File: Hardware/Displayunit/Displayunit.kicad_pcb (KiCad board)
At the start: 4 copper layers, 155 x 64.8 mm, 124 parts, among them IC1 TSC2007, IC2 MX25LM51245GXDI00, IC3 IS66WVH8M8BLL-100B1LI_0, J1 8P8C_Shielded, J2 8P8C_Shielded, J3 54104-4031, J4 Conn_ARM_JTAG_SWD_20, J5 52271-0679, J6 Conn_02x06_Odd_Even, J7 WAGO_Klemmleiste_2-pol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

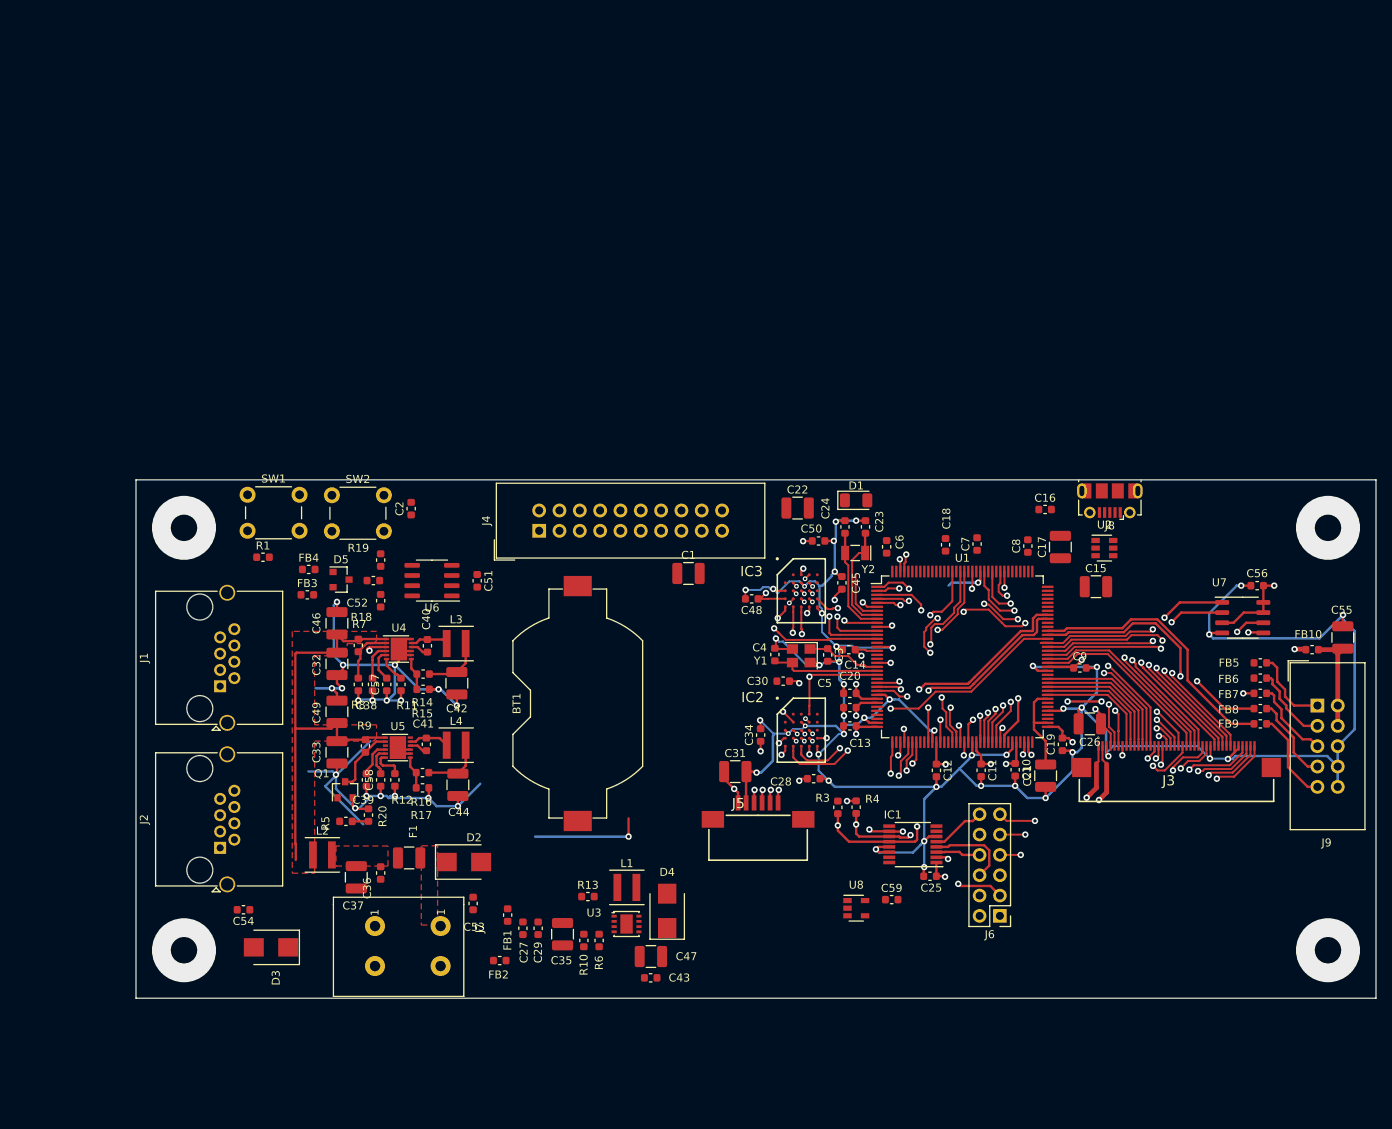
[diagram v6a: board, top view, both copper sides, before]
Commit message: Displayboard fertig layoutet, kleinere Fehler beseitigt, WomoLin Biblothek senkrechter Würth RJ 45 zugefügt
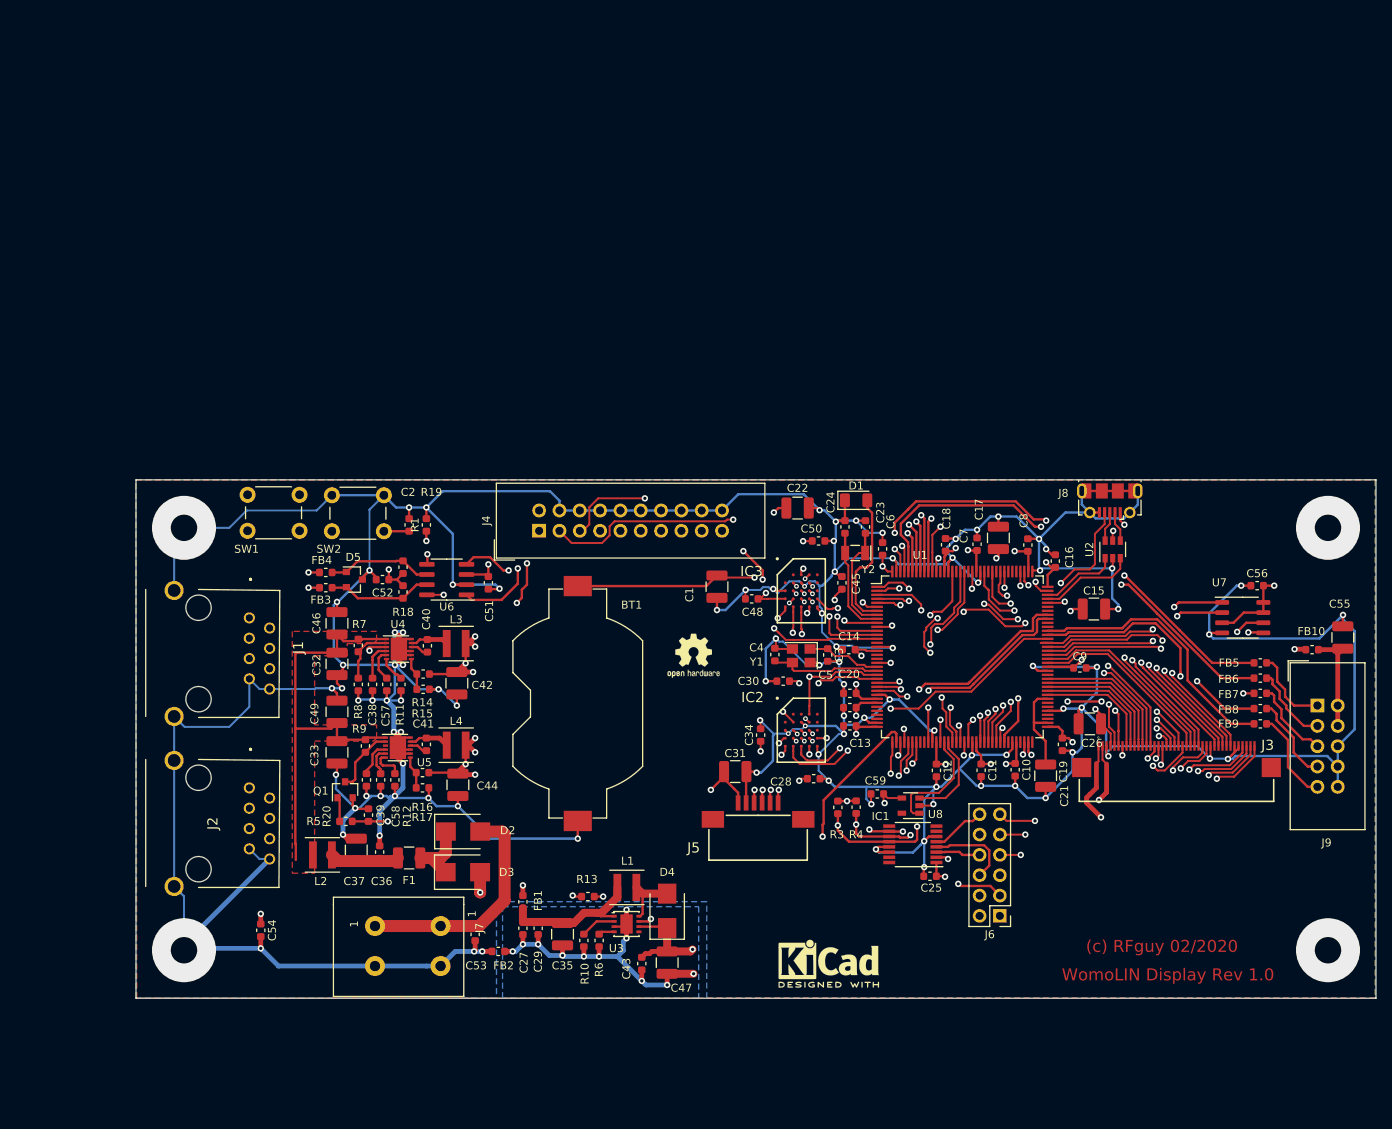
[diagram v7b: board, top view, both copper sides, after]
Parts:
- added REF**: OSHW-Logo2_7.3x6mm_SilkScreen, Symbol:OSHW-Logo2_7.3x6mm_SilkScreen, F.Cu at (131.7, 71.0)
- added REF**: KiCad-Logo2_5mm_SilkScreen, Symbol:KiCad-Logo2_5mm_SilkScreen, F.Cu at (148.6, 109.5)
- IC2: value MX25LM51245GXDI00 -> (none)
- IC3: value IS66WVH8M8BLL-100B1LI_0 -> (none)
- J1, J2: value 8P8C_Shielded -> 615008138221; footprint Connector_RJ:RJ45_Amphenol_RJHSE5380 -> Womo-Lin:615008138221
- J3: value 54104-4031 -> (none)
- J5: value 52271-0679 -> (none)
- moved D3 25.8 mm to (102.9, 98.0), turned to 0 degrees
- moved R1 20.8 mm to (98.3, 54.6), turned to 90 degrees
- moved U8 14.5 mm to (158.8, 89.7), turned to 180 degrees
- moved C59 13.3 mm to (154.7, 88.3), turned to 180 degrees
- moved J1 9.29 mm to (76.2, 66.3), turned to 270 degrees
- moved J2 8.33 mm to (76.2, 87.5), turned to 270 degrees
- moved C17 7.83 mm to (169.8, 56.3)
- moved C16 6.58 mm to (176.9, 59.2), turned to 90 degrees
- moved C1 3.92 mm to (134.6, 62.4), turned to 270 degrees
- moved C53 3.87 mm to (104.4, 105.8)
- moved D2 3.81 mm to (102.9, 93.0)
- moved C37 3.43 mm to (89.5, 95.3), turned to 90 degrees
- moved C54 3.35 mm to (77.6, 105.3), turned to 270 degrees
- moved R18 3.00 mm to (95.4, 63.0)
- moved R19 2.93 mm to (95.4, 59.9)
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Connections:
- U1 pad 135: Wakeup -> 3VA_EN
- U1 pad 24: Net-(U1-Pad24) -> CAN_STB
- U1 pad 38: LCD_BL_CTR -> LCD_BL_CTRL
- U2 pad 1: USB_D- -> USB_D+
- U2 pad 3: USB_D+ -> USB_D-
- U2 pad 4: Net-(J8-Pad3) -> Net-(J8-Pad2)
- U2 pad 6: Net-(J8-Pad2) -> Net-(J8-Pad3)
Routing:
- net GND: track 483.3 -> 889.5 mm, vias 66 -> 99
- net +3V3: track 202.8 -> 408.3 mm, vias 22 -> 36
- net 3VA_EN: track 2.03 -> 110.5 mm, vias 0 -> 4
- net Boot0: track 0.00 -> 100.8 mm, vias 0 -> 2
- net Control+: track 0.00 -> 82.5 mm, vias 0 -> 2
- net JTAG_TMS: track 0.00 -> 71.5 mm, vias 0 -> 1
- net USART1_TX: track 0.00 -> 70.2 mm, vias 0 -> 2
- net JTAG_TDI: track 0.00 -> 70.1 mm, vias 0 -> 2
- net CAN_STB: track 0.00 -> 67.4 mm, vias 0 -> 2
- net USART1_RX: track 0.00 -> 67.1 mm, vias 0 -> 2
- net JTAG_TCK: track 0.00 -> 67.0 mm, vias 0 -> 1
- net +3.3VA: track 87.6 -> 154.3 mm, vias 4 -> 10
- net RESET: track 31.8 -> 96.7 mm, vias 2 -> 5
- net EXT_1: track 0.00 -> 62.8 mm, vias 0 -> 4
- net EXT_2: track 0.00 -> 60.4 mm, vias 0 -> 2
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- added copper zone on In2.Cu, net +3.3VA
- added copper zone on In2.Cu, net +3V3
- added copper zone on B.Cu, net GND
- added copper zone on F.Cu, net GND
- added copper zone on B.Cu, net LCD_LED-K
- removed copper zone on F.Cu, net Net-(C36-Pad1)
- removed copper zone on F.Cu, net Net-(D2-Pad1)
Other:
- board text added: "(c) RFguy 02/2020"
- board text added: "WomoLIN Display Rev 1.0"

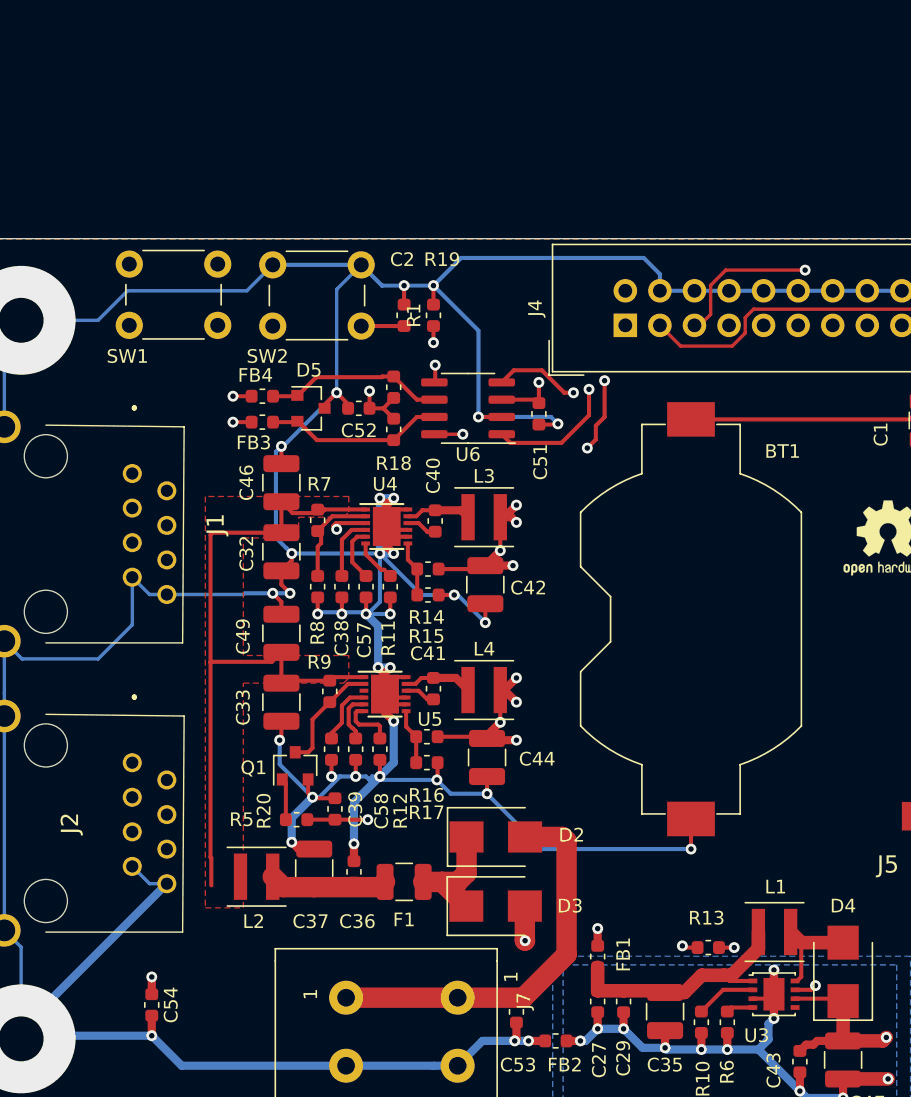
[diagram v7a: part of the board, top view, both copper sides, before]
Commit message: Änderung PSU Displayboard, Lib angepast.
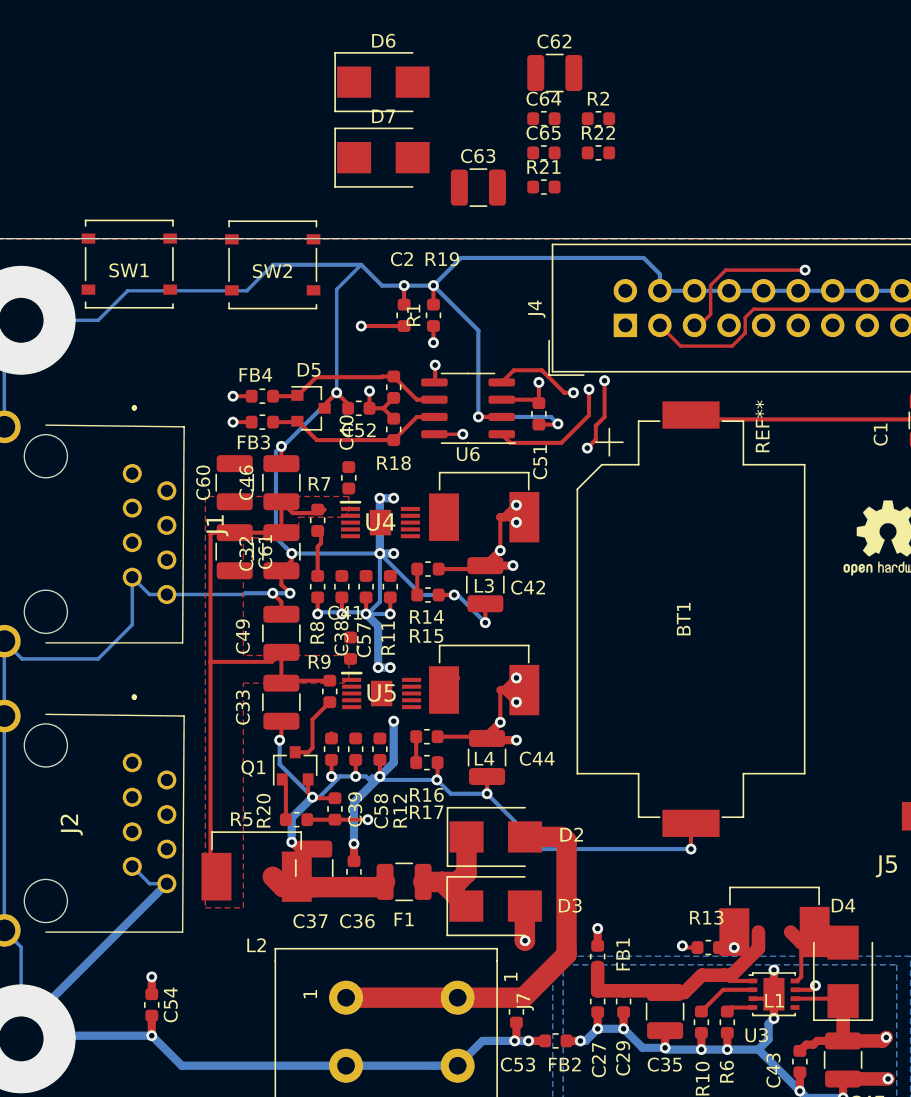
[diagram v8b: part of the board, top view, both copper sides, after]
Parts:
- added C60: 2u2, Capacitor_SMD:C_1210_3225Metric, F.Cu at (83.7, 66.9)
- added C61: 2u2, Capacitor_SMD:C_1210_3225Metric, F.Cu at (83.7, 72.0)
- added C62: 100n, Capacitor_SMD:C_1210_3225Metric, F.Cu at (107.2, 36.8)
- added C63: 100n, Capacitor_SMD:C_1210_3225Metric, F.Cu at (101.6, 45.2)
- added C64: 2n7, Capacitor_SMD:C_0603_1608Metric, F.Cu at (106.4, 40.2)
- added C65: 2n7, Capacitor_SMD:C_0603_1608Metric, F.Cu at (106.4, 42.7)
- added D6: B260A-13-F, Diode_SMD:D_SMB, F.Cu at (94.6, 37.5)
- added D7: B260A-13-F, Diode_SMD:D_SMB, F.Cu at (94.6, 43.0)
- added R2: 10K, Resistor_SMD:R_0603_1608Metric, F.Cu at (110.4, 40.2)
- added R21: 76K8, Resistor_SMD:R_0603_1608Metric, F.Cu at (106.4, 45.2)
- added R22: 76K8, Resistor_SMD:R_0603_1608Metric, F.Cu at (110.4, 42.7)
- BT1: footprint Battery:BatteryHolder_Keystone_1058_1x2032 -> Womo-Lin:QJ.BS-6
- C38, C39: value 5n6 -> 10n
- C40, C41: value 100nF -> 100n
- C44: value 22uF -> 47u
- C57, C58: value 4u7 -> 6p8
- D2, D3: value B250 -> B260A-13-F
- FB10, FB5, FB6, FB7, FB8, FB9: value 100R -> BLM18PG121SN1D
- IC2: value (none) -> MX25LM51245GXDI00
- IC3: value (none) -> IS66WVH8M8BLL-100B1LI_0
- J3: value (none) -> 54104-4031
- J5: value (none) -> 52271-0679
- L1: footprint Inductor_SMD:L_Coilcraft_XxL4030 -> Womo-Lin:MWSA0603
- L2: footprint Inductor_SMD:L_Coilcraft_XxL4020 -> Womo-Lin:MWSA0603
- L3, L4: value 15uH -> 10uH; footprint Inductor_SMD:L_Coilcraft_XxL4040 -> Womo-Lin:MWSA0603
- R11, R12: value 40k2 -> 90k9
- R14: value 86k6 -> 31K6
- R15: value 32k4 -> 10K
- R16: value 86k6 -> 31k6
- R17: value 32k4 -> 10k
- R7: value 3M3 -> 332k
- R8: value 432k -> 61k9
- R9: value 40k2 -> 332k
- SW1, SW2: footprint Button_Switch_THT:SW_PUSH_6mm -> Womo-Lin:TS-1187A
- U4, U5: value MAX17572 -> TPS54160DGQR; footprint Package_DFN_QFN:DFN-12-1EP_3x3mm_P0.5mm_EP2.05x2.86mm -> Womo-Lin:SOP50P490X110-11N
- U6: value SN65HVD231 -> SN65HVD231DR
- U7: value AT25xxx -> AT25SF161-SHD-T
- U8: value 24AA02-OT -> 24AA02E48T-I/OT
- Y1: value 16 MHz -> X322516MLB4SI
- Y2: value 32.768 -> Q13FC1350000400
- moved C40 7.10 mm to (92.1, 66.6)
- moved C41 6.78 mm to (92.2, 79.1)
- moved U4 0.54 mm to (94.4, 69.9)
- moved U5 0.25 mm to (94.5, 82.4)
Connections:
- U4 pad 1: +BATT -> Net-(C40-Pad2)
- U4 pad 10: Net-(C40-Pad2) -> Net-(C40-Pad1)
- U4 pad 11: Net-(C40-Pad1) -> GND
- U4 pad 2: Net-(R7-Pad2) -> +BATT
- U4 pad 3: PWR_Reset -> Net-(R7-Pad2)
- U4 pad 5: Net-(C57-Pad2) -> Net-(R11-Pad1)
- U4 pad 6: Net-(R11-Pad1) -> PWR_Reset
- U4 pad 8: GND -> Net-(C57-Pad2)
- U5 pad 1: +BATT -> Net-(C41-Pad2)
- U5 pad 10: Net-(C41-Pad2) -> Net-(C41-Pad1)
- U5 pad 11: Net-(C41-Pad1) -> GND
- U5 pad 2: Net-(Q1-Pad3) -> +BATT
- U5 pad 3: Net-(U5-Pad3) -> Net-(Q1-Pad3)
- U5 pad 5: Net-(C58-Pad2) -> Net-(R12-Pad1)
- U5 pad 6: Net-(R12-Pad1) -> Net-(U5-Pad6)
- U5 pad 8: GND -> Net-(C58-Pad2)
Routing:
- net GND: track 889.5 -> 860.3 mm
- net +BATT: track 54.0 -> 48.8 mm
- net Net-(C40-Pad1): track 4.82 -> 0.00 mm
- net Net-(C38-Pad1): track 4.71 -> 0.00 mm
- net Net-(C39-Pad1): track 4.59 -> 0.38 mm
- net Net-(R12-Pad1): track 4.11 -> 0.00 mm
- net Net-(C57-Pad2): track 4.08 -> 0.00 mm
- net Net-(R7-Pad2): track 7.13 -> 3.15 mm
- net Net-(C58-Pad2): track 3.68 -> 0.00 mm
- net Net-(C41-Pad1): track 5.10 -> 1.65 mm
- net Net-(R11-Pad1): track 3.26 -> 0.00 mm
- net Net-(Q1-Pad3): track 8.41 -> 5.34 mm
- net PWR_Reset: track 2.59 -> 0.00 mm, vias 1 -> 0
- net Net-(C41-Pad2): track 2.27 -> 0.00 mm
- net Net-(C40-Pad2): track 2.27 -> 0.00 mm
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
